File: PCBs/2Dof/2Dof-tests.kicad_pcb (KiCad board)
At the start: 2 copper layers, 53.3 x 46 mm, 45 parts, among them J1 Conn_02x07_Odd_Even, J12 RS485, J14 HBA, J17 Servo1, J2 Conn_02x08_Odd_Even, J3 Conn_02x08_Odd_Even, J5 24Vin, J9 Laser Diode, Q1 QServoA, Q6 LaserDiodeT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

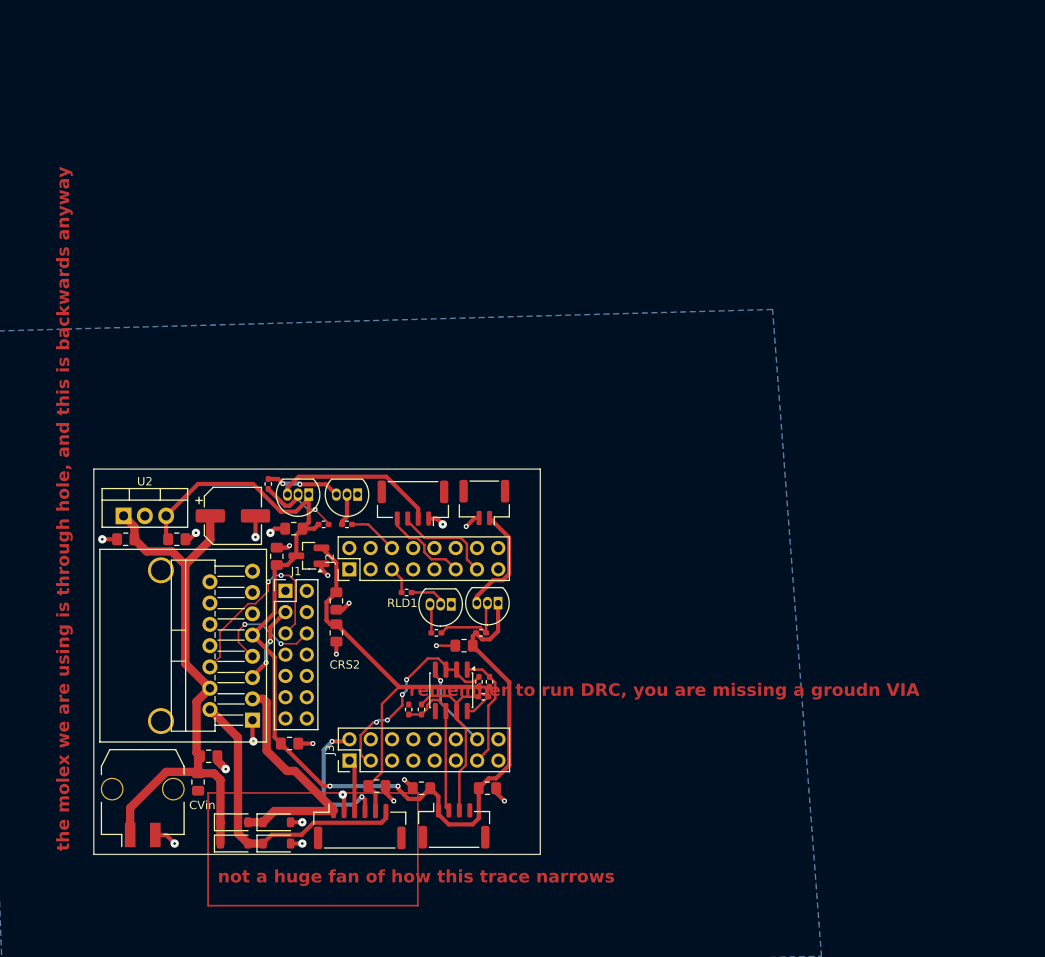
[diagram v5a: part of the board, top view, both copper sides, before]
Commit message: new 5V reg
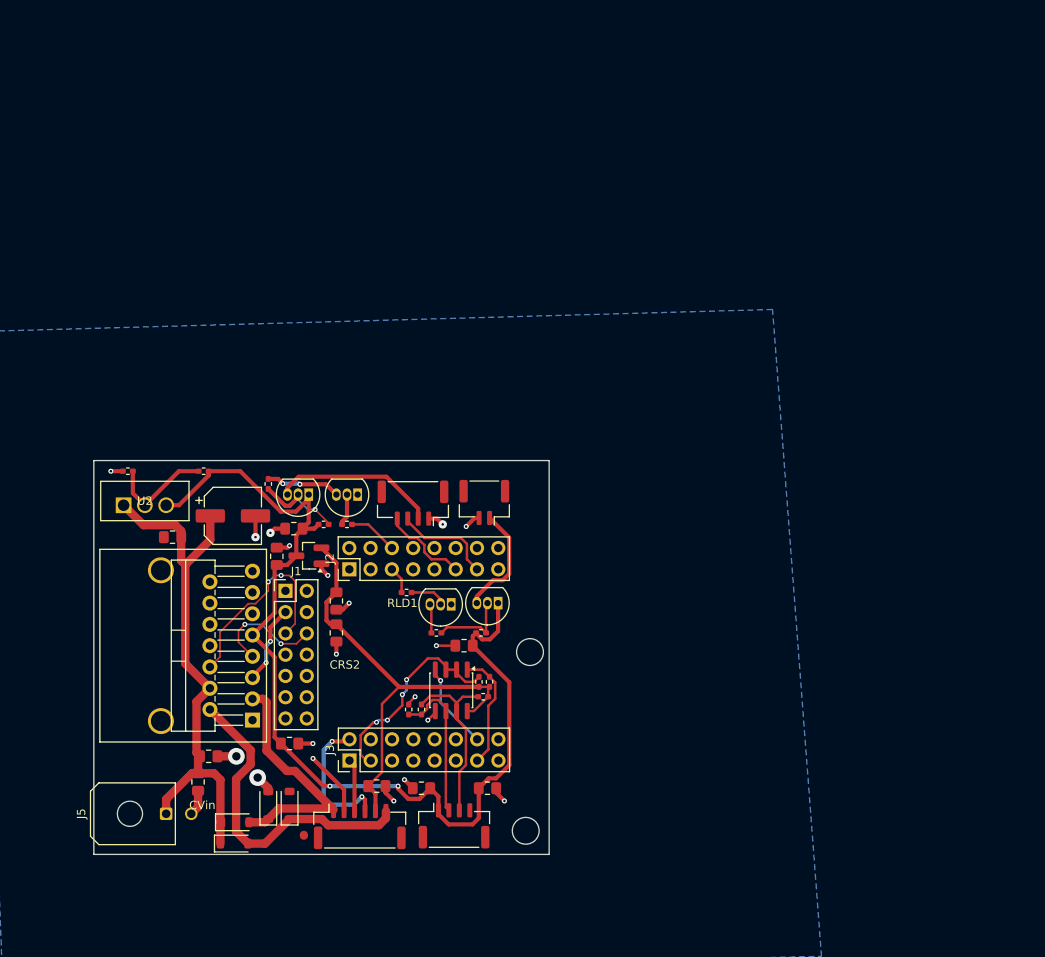
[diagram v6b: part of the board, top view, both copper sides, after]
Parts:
- removed CVregA2: 100n, Capacitor_SMD:C_0805_2012Metric_Pad1.18x1.45mm_HandSolder
- added H1: MountingHole, MountingHole:MountingHole_3.2mm_M3, F.Cu at (155.4, 66.5)
- added H2: MountingHole, MountingHole:MountingHole_3.2mm_M3, F.Cu at (154.9, 87.9)
- added RLD5: 220, Resistor_SMD:R_0402_1005Metric_Pad0.72x0.64mm_HandSolder, F.Cu at (116.5, 45.0)
- added RServoA6: 680, Resistor_SMD:R_0402_1005Metric_Pad0.72x0.64mm_HandSolder, F.Cu at (107.4, 45.0)
- J5: footprint Connector_Molex:Molex_Micro-Fit_3.0_43650-0210_1x02-1MP_P3.00mm_Horizontal -> Connector_Molex:Molex_Micro-Fit_3.0_43045-0200_2x01_P3.00mm_Horizontal
- U2: footprint Package_TO_SOT_THT:TO-220-3_Vertical -> footprints:T03B
- moved CVregA1 5.59 mm to (112.8, 52.8)
- moved U2 5.57 mm to (112.0, 48.0)
- moved DHBA2 4.82 mm to (126.7, 84.8), turned to 90 degrees
- moved J5 3.81 mm to (112.0, 85.9), turned to 90 degrees
- moved DHBA4 2.27 mm to (124.2, 84.8), turned to 90 degrees
- moved DHBA3 0.13 mm to (120.3, 86.9)
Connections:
- U2 pad 2: GND -> Net-(U2-GND)
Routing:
- net Net-(U2-GND): track 0.00 -> 12.8 mm
- net +24V: track 68.6 -> 64.2 mm
- net GND: track 40.7 -> 44.4 mm, vias 21 -> 19
- net Net-(DHBA1-A): track 36.5 -> 38.5 mm
- net +5V: track 124.4 -> 122.6 mm
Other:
- board size 53.3 x 46 mm -> 54.4 x 47 mm
- board text removed: "not a huge fan of how this trace narrows"
- board text removed: "remember to run DRC, you are missing a groudn VIA"
- board text removed: "the molex we are using is through hole, and this is backwards anyway"

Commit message: make it look beautiful
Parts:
- renumbered J5 to 24Vin
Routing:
- net GND: track 44.4 -> 53.0 mm, vias 19 -> 21
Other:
- board text added: "AMT"
- board text added: "DC"
- board text added: "G"
- board text added: "like this"
- board text added: "or liek this"
- board text added: "what do i even do for pinouts?"
- board text removed: "In the box I made, the routings not great, a lot of places have vias where they dont need if the routing and placement was done better. An example of this is the resistor for the transciever (RRS4?)--ok Is super far away from the transciever so it leads to you using vias where not needed -- ok you should have a 10uf at the 24V input header, also you should move it further from the hbridge since t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"
- board text removed: "RUN DRC, you are missing some ground VIAS Vias go through layers, throughhole components already go thgrough the layers If you look at the shaded blue part, you'll see theres no {dblquote}bubble{dblquote} around tht components that need ground, there is a t shape through them, so they are already connected to ground. Only surface mount pads need them since they need some way to get the ground con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"
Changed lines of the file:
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@@
 		(tags "capacitor handsolder")
 		(property "Reference" "CVin"
-			(at 2.7725 -0.508 180)
+			(at 6.3285 0 180)
 			(layer "F.SilkS")
+			(hide yes)
 			(effects
 				(font
@@
 		(tags "LM1085IT-5.0/NOPB ")
 		(property "Reference" "U2"
-			(at -2.54 0.508 0)
+			(at -2.54 2.8575 0)
 			(unlocked yes)
 			(layer "F.SilkS")
+			(hide yes)
 			(effects
 				(font
@@
 			(at -3.81 1.016 180)
 			(layer "F.SilkS")
+			(hide yes)
 			(effects
 				(font
@@
 		(descr "Molex Micro-Fit 3.0 Connector System, 43045-0200 (alternative finishes: 43045-020x), 1 Pins per row (https://www.molex.com/pdm_docs/sd/430450201_sd.pdf), generated with kicad-footprint-generator")
 		(tags "connector Molex Micro-Fit_3.0 horizontal")
-		(property "Reference" "J5"
-			(at 0 -10.12 90)
+		(property "Reference" "24Vin"
+			(at 5.08 -4.572 180)
 			(layer "F.SilkS")
 			(effects
@@
 		(layer "Edge.Cuts")
 	)
-	(gr_text "RUN DRC, you are missing some ground VIAS\n\nVias go through layers, throughhole components already go thgrough the layers\nIf you look at the shaded blue part, you'll see theres no {dblquote}bubble{dblquote} around\ntht components that need ground, there is a t shape through them, so they are\nalready connected to ground. Only surface mount pads need them since they\nneed some way to get the ground connection\n\nthe traces going to the motor should be much much thicker, the traces\nThe traces going to the servos and any high current carrying routes\nshould be thicker as well. Similalry if you have a wider trace, you need \na wider via, the via hole should = trace width, and the via diamter should be double\nalso if you have a capacitor with a thick power trace, the ground trace\nshould be equally as thick\n\nConstraints are in the board setup tab... also google... :(\n\nclean up silkscreen by removing the stuff u dont need and putting\nhelpful labels that will make it easy to assemble and use\n\nAlso changr the jst to the standard one we are using\n\nalso avoid 90 degree traces, also the 5V trace in the big square\ni highlighted is super wonky, i dont think it needs to be like that\n\nPlease go through and clean up some traces, you have vias where you \ndont need them like in the smaller square I made, just comb through \nall of em and make sure theres no unnecessary vias, or if there is a \nbetter way to route that specific area\n\nAre u sure U2 has the right footprint, usually vregs are smd?"
-		(at -113.792 151.892 0)
-		(layer "F.Cu")
+	(gr_text "like this \n"
+		(at 143.51 42.418 0)
+		(layer "F.SilkS")
+		(effects
+			(font
+				(size 1 1)
+				(thickness 0.1)
+			)
+			(justify left bottom)
+		)
+	)
+	(gr_text "DC"
+		(at 133.858 89.662 0)
+		(layer "F.SilkS")
+		(effects
+			(font
+				(size 1 1)
+				(thickness 0.1)
+			)
+			(justify left bottom)
+		)
+	)
+	(gr_text "or liek this"
+		(at 136.906 93.472 0)
+		(layer "F.SilkS")
+		(effects
+			(font
+				(size 1 1)
+				(thickness 0.1)
+			)
+			(justify left bottom)
+		)
+	)
+	(gr_text "what do i even do for pinouts?"
+		(at 137.922 37.846 0)
+		(layer "F.SilkS")
+		(effects
+			(font
+				(size 1 1)
+				(thickness 0.1)
+			)
+			(justify left bottom)
+		)
+	)
+	(gr_text "G"
+		(at 144.272 44.196 180)
+		(layer "F.SilkS")
+		(effects
+			(font
+				(size 1 1)
+				(thickness 0.1)
+			)
+			(justify left bottom)
+		)
+	)
+	(gr_text "AMT"
+		(at 145.034 89.408 0)
+		(layer "F.SilkS")
 		(effects
 			(font
-				(size 1.5 1.5)
-				(thickness 0.3)
-				(bold yes)
+				(size 1 1)
+				(thickness 0.1)
 			)
 			(justify left bottom)
 		)
 	)
-	(gr_text "In the box I made, the routings not great, a lot of places have vias where they dont need if the\nrouting and placement was done better. An example of this is the resistor for the transciever (RRS4?)--ok\nIs super far away from the transciever so it leads to you using vias where not needed -- ok\n\nyou should have a 10uf at the 24V input header, also you should move it further from the hbridge since the \nheatsink will overlap, if you turn on silkscreen you should see it -- ok\n\nif smth is tht and connected to GND, it doesnt need a via -- plz clarify i thought u needed to connect everything to gnd via vias\n\nSuper important: ur constraints are not set up right, so it might show that it \npasses the DRC, but the DRC is just wrong if the constraints are wrong\n-- how do i setup constraints\n\nlater:\nclean up silkscreen, add pinouts on the silkscreen\n-- how do i clean up silkscreen "
-		(at -114.046 45.466 0)
-		(layer "User.1")
+	(gr_text "G"
+		(at 149.606 44.196 180)
+		(layer "F.SilkS")
 		(effects
 			(font
 				(size 1 1)
-				(thickness 0.15)
+				(thickness 0.1)
 			)
 			(justify left bottom)
@@
 	)
 	(segment
-		(start 128.453 88.375)
-		(end 128.453 88.463)
-		(width 1)
-		(layer "F.Cu")
-		(net 15)
-	)
-	(segment
 		(start 133.0745 61.4895)
 		(end 133.858 60.706)
@@
 	)
 	(segment
+		(start 148.264 83.658)
+		(end 147.664 83.058)
+		(width 0.3)
+		(layer "F.Cu")
+		(net 15)
+	)
+	(segment
 		(start 151.4055 82.804)
 		(end 151.4055 83.3335)
@@
 	)
 	(segment
+		(start 111.7385 52.832)
+		(end 108.204 52.832)
+		(width 1)
+		(layer "F.Cu")
+		(net 15)
+	)
+	(segment
 		(start 138.1975 83.3335)
 		(end 139.192 84.328)
@@
 	)
 	(segment
+		(start 126.746 83.186)
+		(end 124.206 83.186)
+		(width 1)
+		(layer "F.Cu")
+		(net 15)
+	)
+	(segment
 		(start 141.4565 82.7825)
 		(end 140.462 81.788)
@@
 	)
 	(segment
+		(start 148.264 85.446)
+		(end 148.264 83.658)
+		(width 0.3)
+		(layer "F.Cu")
+		(net 15)
+	)
+	(segment
 		(start 133.253 82.961)
 		(end 129.54 79.248)
@@
 	)
 	(via
+		(at 108.204 52.832)
+		(size 2)
+		(drill 1)
+		(layers "F.Cu" "B.Cu")
+		(net 15)
+	)
+	(via
 		(at 126.746 53.848)
 		(size 0.6)
@@
 		(size 0.6)
 		(drill 0.3)
+		(layers "F.Cu" "B.Cu")
+		(net 15)
+	)
+	(via
+		(at 147.664 83.058)
+		(size 0.6)
+		(drill 0.3)

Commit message: comments, ignore
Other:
- board text added: "what do i even do for pinouts? yeah on the silkscreen, like for a servo you'd label which is power, gnd, pwm, etc or like for the encoder you would label power, gnd, A, B"
- board text removed: "what do i even do for pinouts?"
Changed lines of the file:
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@@
 		)
 	)
-	(gr_text "what do i even do for pinouts?"
+	(gr_text "what do i even do for pinouts?\n\nyeah on the silkscreen, like for a servo you'd label which is power, gnd, pwm, etc\nor like for the encoder you would label power, gnd, A, B"
 		(at 137.922 37.846 0)
 		(layer "F.SilkS")
